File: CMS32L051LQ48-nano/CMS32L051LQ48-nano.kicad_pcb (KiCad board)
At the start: 4 copper layers, 18 x 43.2 mm, 31 parts, among them J101 Board Pin, J102 Board Pin, J103 USB_B_Micro, J105 Connection to DAPLink Board, U201 CMS32L051LQ48, U301 AP2127K-ADJ

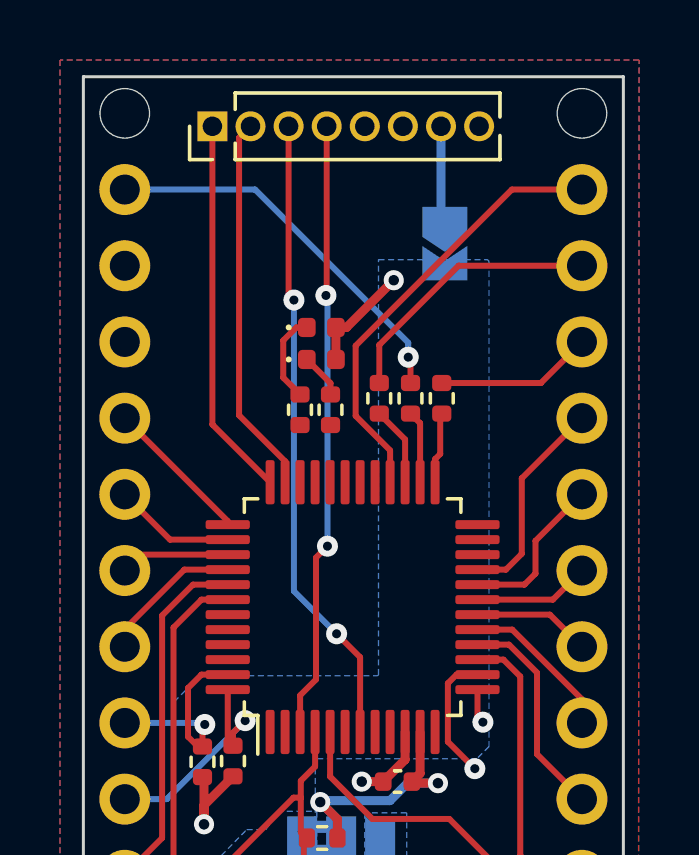
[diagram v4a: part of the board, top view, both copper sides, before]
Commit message: fix DRCs
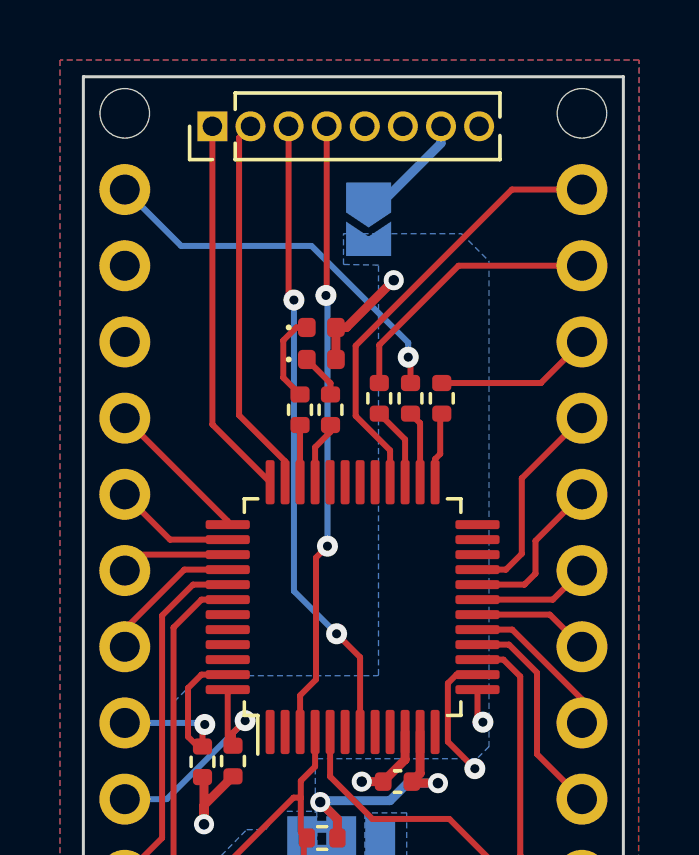
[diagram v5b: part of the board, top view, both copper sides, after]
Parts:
- moved JP102 2.67 mm to (99.8, 53.4)
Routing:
- net /MCU/LED2: track 0.00 -> 2.12 mm
- net /MCU/LED1: track 0.00 -> 1.91 mm
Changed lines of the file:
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@@
     (descr "KiCad Logo")
     (tags "Logo KiCad")
-    (attr exclude_from_pos_files exclude_from_bom)
+    (attr board_only exclude_from_pos_files exclude_from_bom)
     (fp_text reference "REF**" (at 0 5.08 90) (layer "B.SilkS") hide
         (effects (font (size 1 1) (thickness 0.15)) (justify mirror))
@@
   )
   (footprint "Jumper:SolderJumper-2_P1.3mm_Open_TrianglePad1.0x1.5mm" (layer "B.Cu")
-    (at 102.362 54.2544 -90)
+    (at 99.822 53.4416 -90)
     (descr "SMD Solder Jumper, 1x1.5mm Triangular Pads, 0.3mm gap, open")
     (tags "solder jumper open")
@@
     (effects (font (size 1 1) (thickness 0.15)) (justify left bottom mirror))
   )
-  (gr_text "D12" (at 104.9782 52.5018) (layer "B.SilkS")
+  (gr_text "D12" (at 104.9274 53.1876) (layer "B.SilkS")
     (effects (font (size 1 1) (thickness 0.15)) (justify left bottom mirror))
   )
@@
     (effects (font (size 1 1) (thickness 0.15)) (justify left bottom mirror))
   )
-  (gr_text "D11" (at 104.775 53.3146 90) (layer "B.SilkS")
+  (gr_text "D11" (at 104.8258 55.6006) (layer "B.SilkS")
     (effects (font (size 1 1) (thickness 0.15)) (justify left bottom mirror))
   )
@@
     (effects (font (size 1 1) (thickness 0.15)) (justify left bottom mirror))
   )
-  (gr_text "RegV_{OUT}" (at 99.8728 55.4228) (layer "B.SilkS")
+  (gr_text "RegV_{OUT}" (at 99.6696 56.3118) (layer "B.SilkS")
     (effects (font (size 1 1) (thickness 0.15)) (justify left bottom mirror))
   )
@@
   (segment (start 101.219 58.9006) (end 101.219 58.1152) (width 0.2) (layer "F.Cu") (net 36))
   (via (at 101.1428 58.039) (size 0.7) (drill 0.3) (layers "F.Cu" "B.Cu") (net 36))
-  (segment (start 96.0374 52.451) (end 91.694 52.451) (width 0.2) (layer "B.Cu") (net 36))
-  (segment (start 101.1428 57.5564) (end 96.0374 52.451) (width 0.2) (layer "B.Cu") (net 36))
   (segment (start 101.1428 58.039) (end 101.1428 57.5564) (width 0.2) (layer "B.Cu") (net 36))
+  (segment (start 97.917 54.3306) (end 93.5736 54.3306) (width 0.2) (layer "B.Cu") (net 36))
+  (segment (start 93.5736 54.3306) (end 91.694 52.451) (width 0.2) (layer "B.Cu") (net 36))
+  (segment (start 101.1428 57.5564) (end 97.917 54.3306) (width 0.2) (layer "B.Cu") (net 36))
   (segment (start 101.5386 62.2077) (end 101.5386 60.2402) (width 0.2) (layer "F.Cu") (net 37))
   (segment (start 101.5386 60.2402) (end 101.219 59.9206) (width 0.2) (layer "F.Cu") (net 37))
@@
   (segment (start 98.0902 85.2546) (end 98.0018 85.1662) (width 0.4) (layer "F.Cu") (net 43))
   (segment (start 98.0902 87.6024) (end 98.0902 85.2546) (width 0.4) (layer "F.Cu") (net 43))
-  (segment (start 102.362 53.5294) (end 102.235 53.4024) (width 0.3) (layer "B.Cu") (net 47))
-  (segment (start 102.235 53.4024) (end 102.235 50.3428) (width 0.3) (layer "B.Cu") (net 47))
+  (segment (start 102.235 50.9132) (end 102.235 50.3428) (width 0.3) (layer "B.Cu") (net 47))
+  (segment (start 100.0252 53.123) (end 102.235 50.9132) (width 0.3) (layer "B.Cu") (net 47))
   (segment (start 101.0386 60.7816) (end 100.1776 59.9206) (width 0.2) (layer "F.Cu") (net 48))
   (segment (start 101.0386 62.2077) (end 101.0386 60.7816) (width 0.2) (layer "F.Cu") (net 48))
@@
   (segment (start 98.552 58.905) (end 97.7622 58.1152) (width 0.2) (layer "F.Cu") (net 61))
   (segment (start 98.552 59.2816) (end 98.552 58.905) (width 0.2) (layer "F.Cu") (net 61))
+  (segment (start 97.536 62.2051) (end 97.5386 62.2077) (width 0.2) (layer "F.Cu") (net 62))
+  (segment (start 97.536 60.3016) (end 97.536 62.2051) (width 0.2) (layer "F.Cu") (net 62))
+  (segment (start 98.0386 61.0416) (end 98.0386 62.2077) (width 0.2) (layer "F.Cu") (net 63))
+  (segment (start 98.552 60.3016) (end 98.552 60.5282) (width 0.2) (layer "F.Cu") (net 63))
+  (segment (start 98.552 60.5282) (end 98.0386 61.0416) (width 0.2) (layer "F.Cu") (net 63))
   (zone (net 3) (net_name "/V_{IN}") (layer "F.Cu") (name "V_in") (hatch edge 0.5)
     (priority 25)
@@
         (xy 100.1268 68.6562)
         (xy 100.1522 68.6308)
-        (xy 100.1522 54.7878)
-        (xy 103.7844 54.7878)
+        (xy 100.1522 54.969431)
+        (xy 98.9838 54.94876)
+        (xy 98.9838 53.9242)
+        (xy 102.9208 53.9242)
         (xy 103.8352 54.8386)
         (xy 103.8352 71.0184)

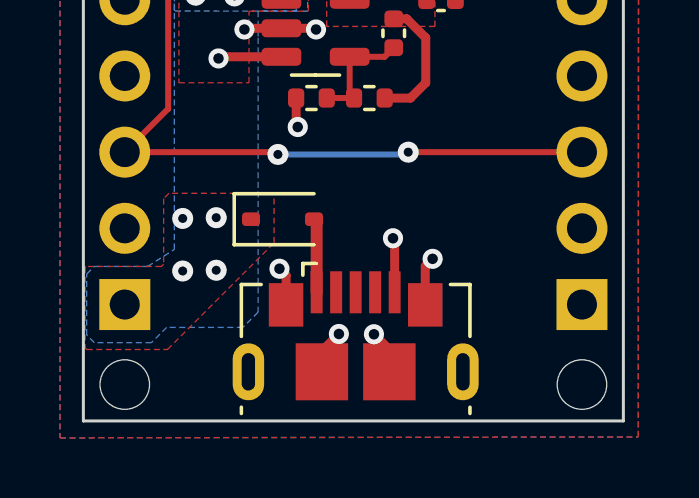
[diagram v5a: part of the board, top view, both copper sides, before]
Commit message: Changed USB micro B connector
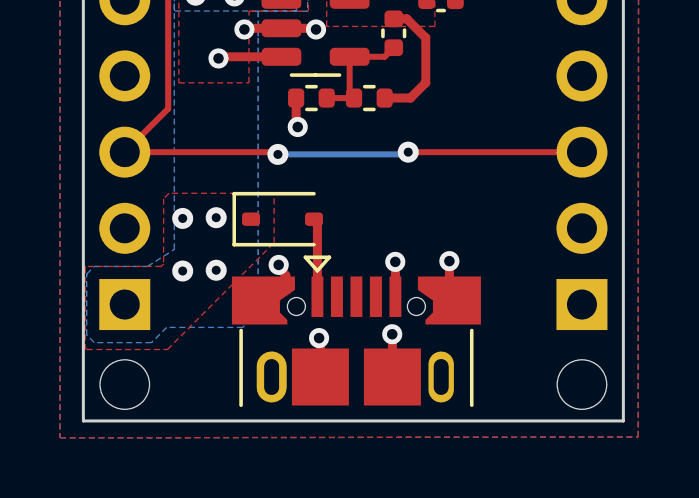
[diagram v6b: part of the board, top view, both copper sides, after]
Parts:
- J103: footprint Connector_USB:USB_Micro-B_GCT_USB3076-30-A -> Connector_USB:USB_Micro-B_XKB_U254-051T-4BH83-F1S
- moved J103 0.98 mm to (99.4, 90.0)
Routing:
- net GND: track 15.0 -> 13.0 mm

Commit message: added revision text
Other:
- board text added: "20230808"
- board text added: "CMS32L051"
- board text added: "REV 1"
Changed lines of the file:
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@@
     (effects (font (size 1 1) (thickness 0.15)) (justify left bottom mirror))
+  )
+  (gr_text "REV 1" (at 94.9452 55.2958) (layer "F.SilkS")
+    (effects (font (size 1 1) (thickness 0.15)) (justify left bottom))
+  )
+  (gr_text "CMS32L051" (at 94.7166 53.6956) (layer "F.SilkS")
+    (effects (font (size 1 1) (thickness 0.15)) (justify left bottom))
+  )
+  (gr_text "20230808" (at 105.8418 59.7916 90) (layer "F.SilkS")
+    (effects (font (size 1 1) (thickness 0.15)) (justify left bottom))
   )
   (dimension (type aligned) (layer "B.Cu")
